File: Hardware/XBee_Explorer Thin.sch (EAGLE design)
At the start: 65 parts, among them J4 QWIIC_RIGHT_ANGLE, Q2 3.1A/30V/105mΩ, U1 FSUSB30MUX_MSOP10, U2 AP63203, U3 ESD Diode, U5 ESD Diode, U6 CP210X

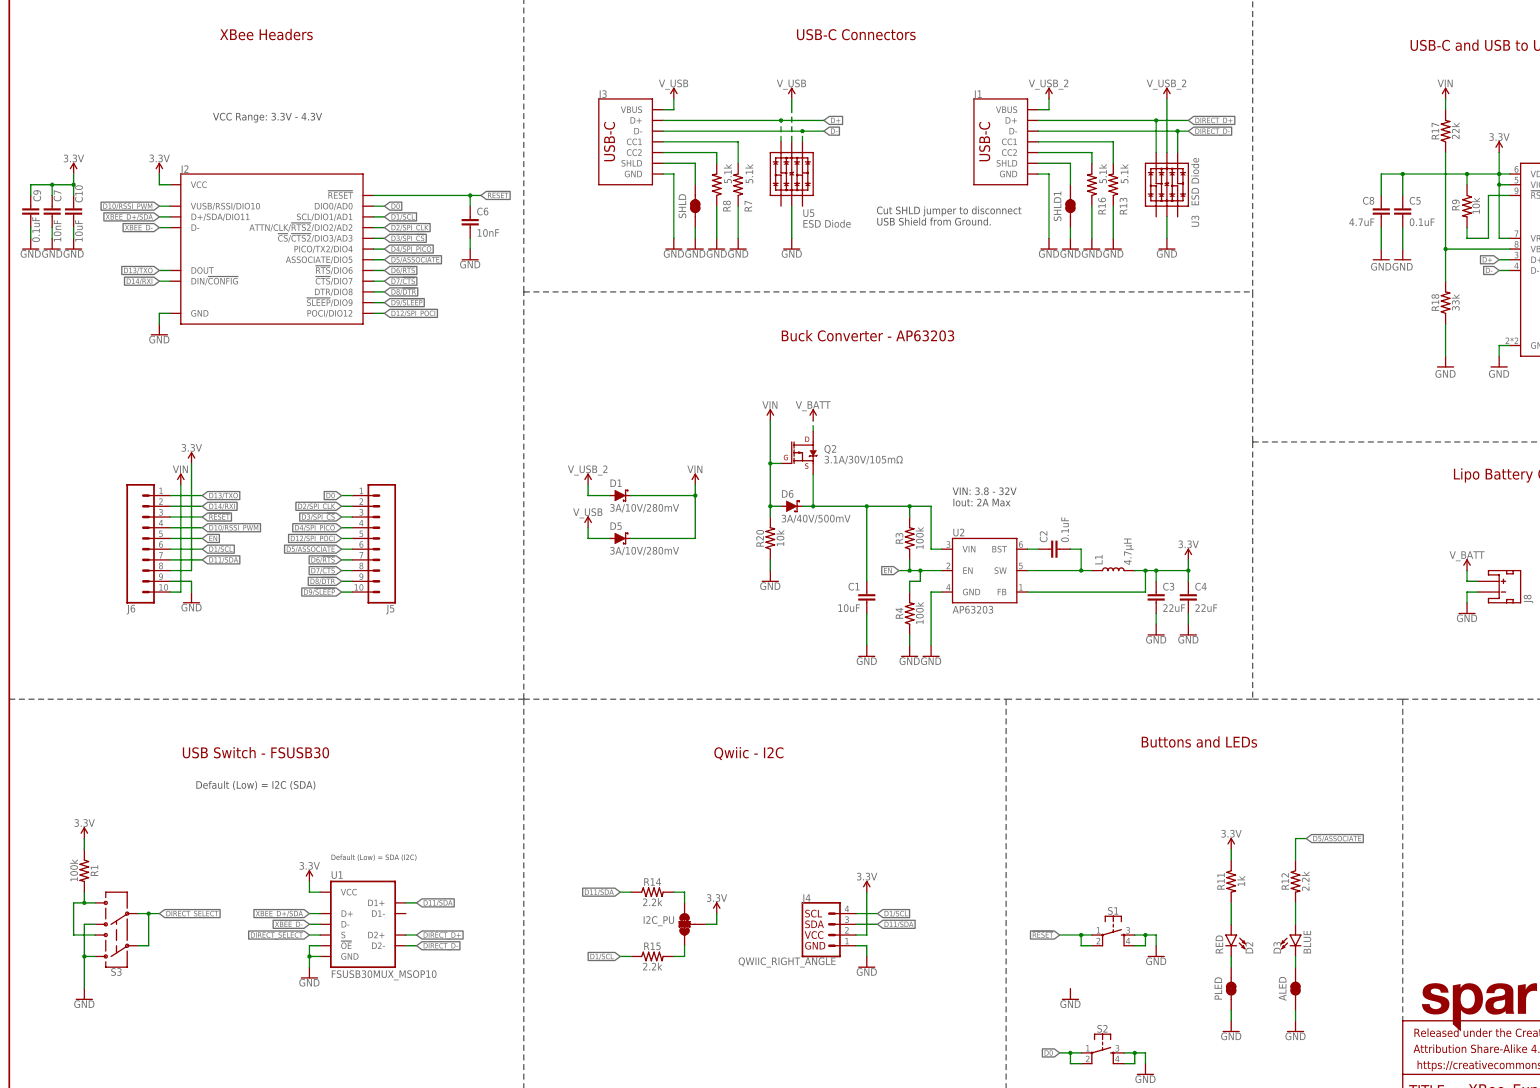
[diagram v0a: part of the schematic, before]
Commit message: Fixes various schematic issues
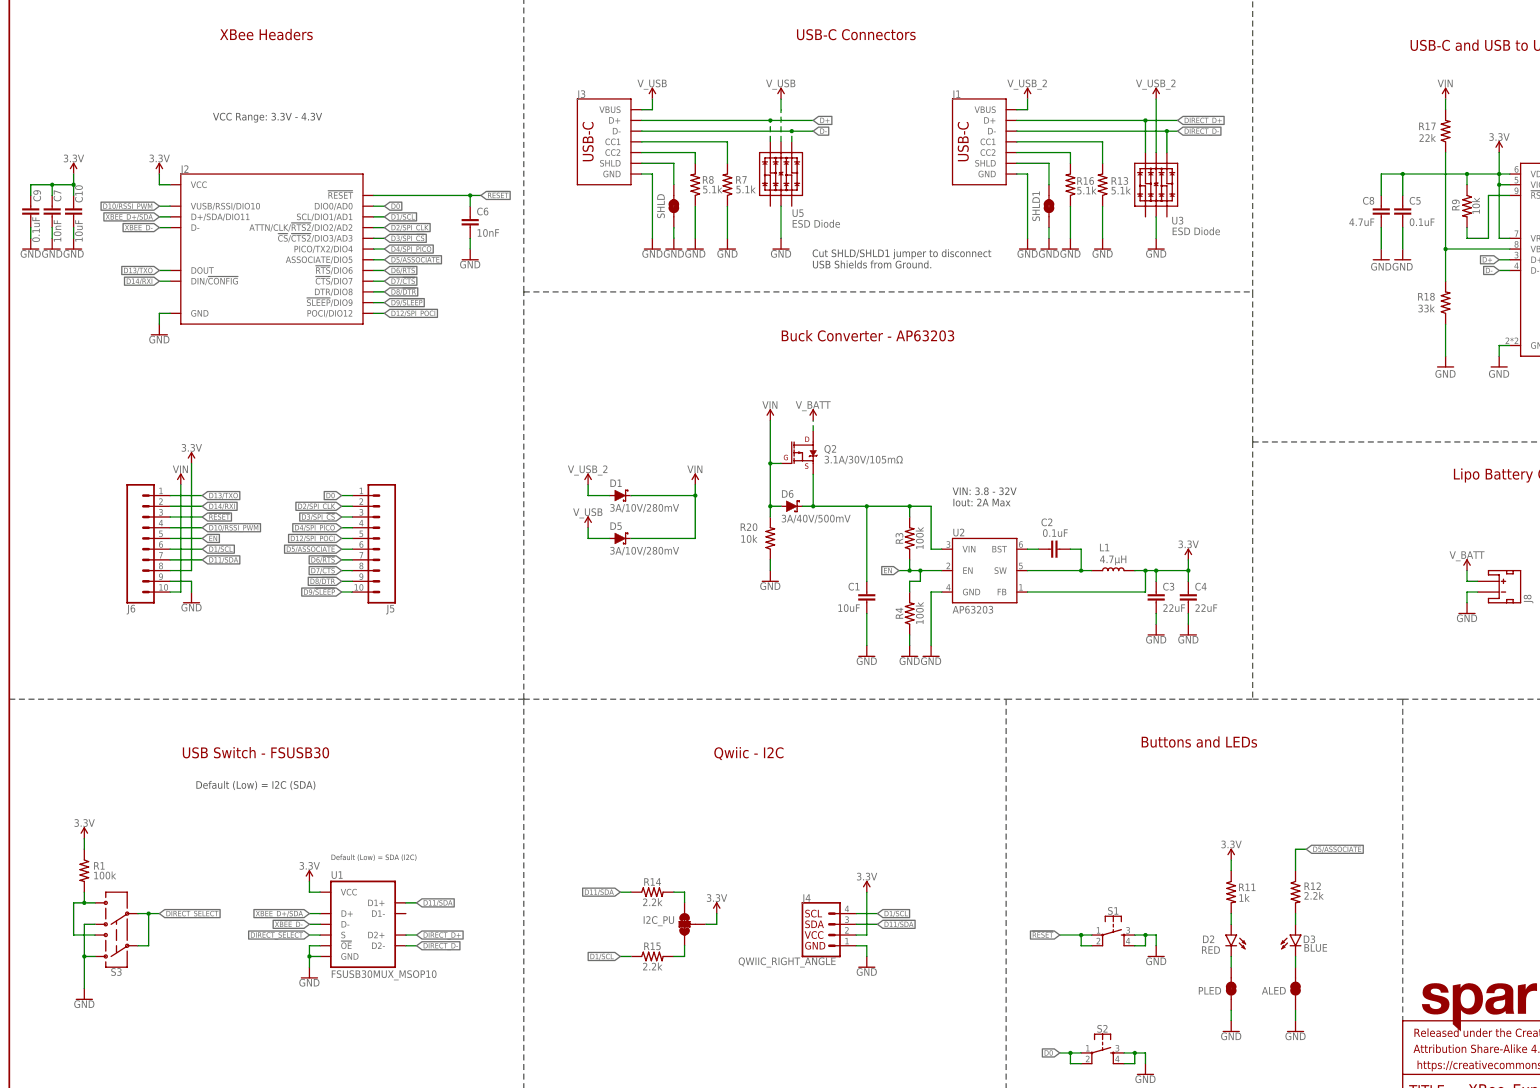
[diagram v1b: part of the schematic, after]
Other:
- note added: "Cut SHLD/SHLD1 jumper to disconnect USB Shields from Ground."
- note removed: "Cut SHLD jumper to disconnect USB Shield from Ground."
- moved on the sheet: J1, J3, R11, R12, R13, R16, R7, R8, SHLD, SHLD1, U3, U5

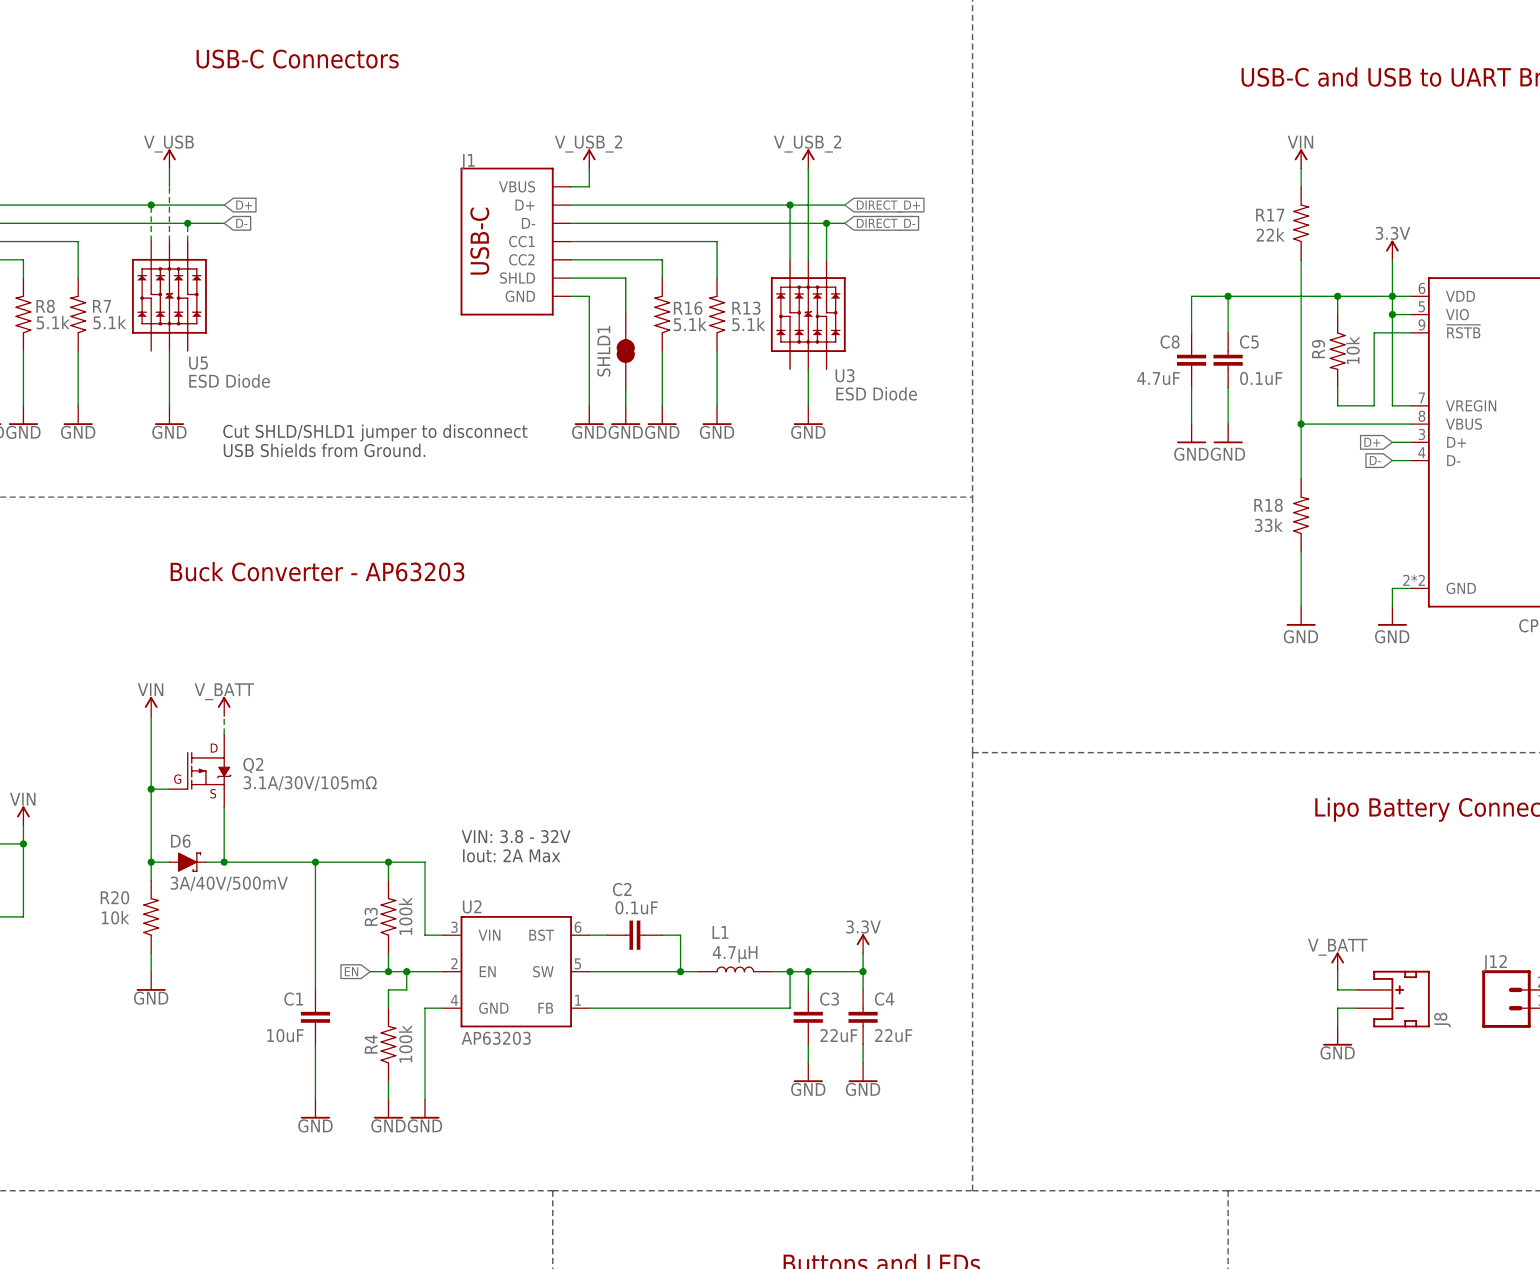
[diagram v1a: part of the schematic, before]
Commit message: Adds more direct feeback trace for feedback pin on regulator
* Restricts ground pour underneath the inductor (which still needs to be changed)
* Updates USB lines to get closer to a 90 ohm impedance (8 mil, 6mil spacing)
* Removes voltage divider on EN pin that was changing the UVLO threshold.
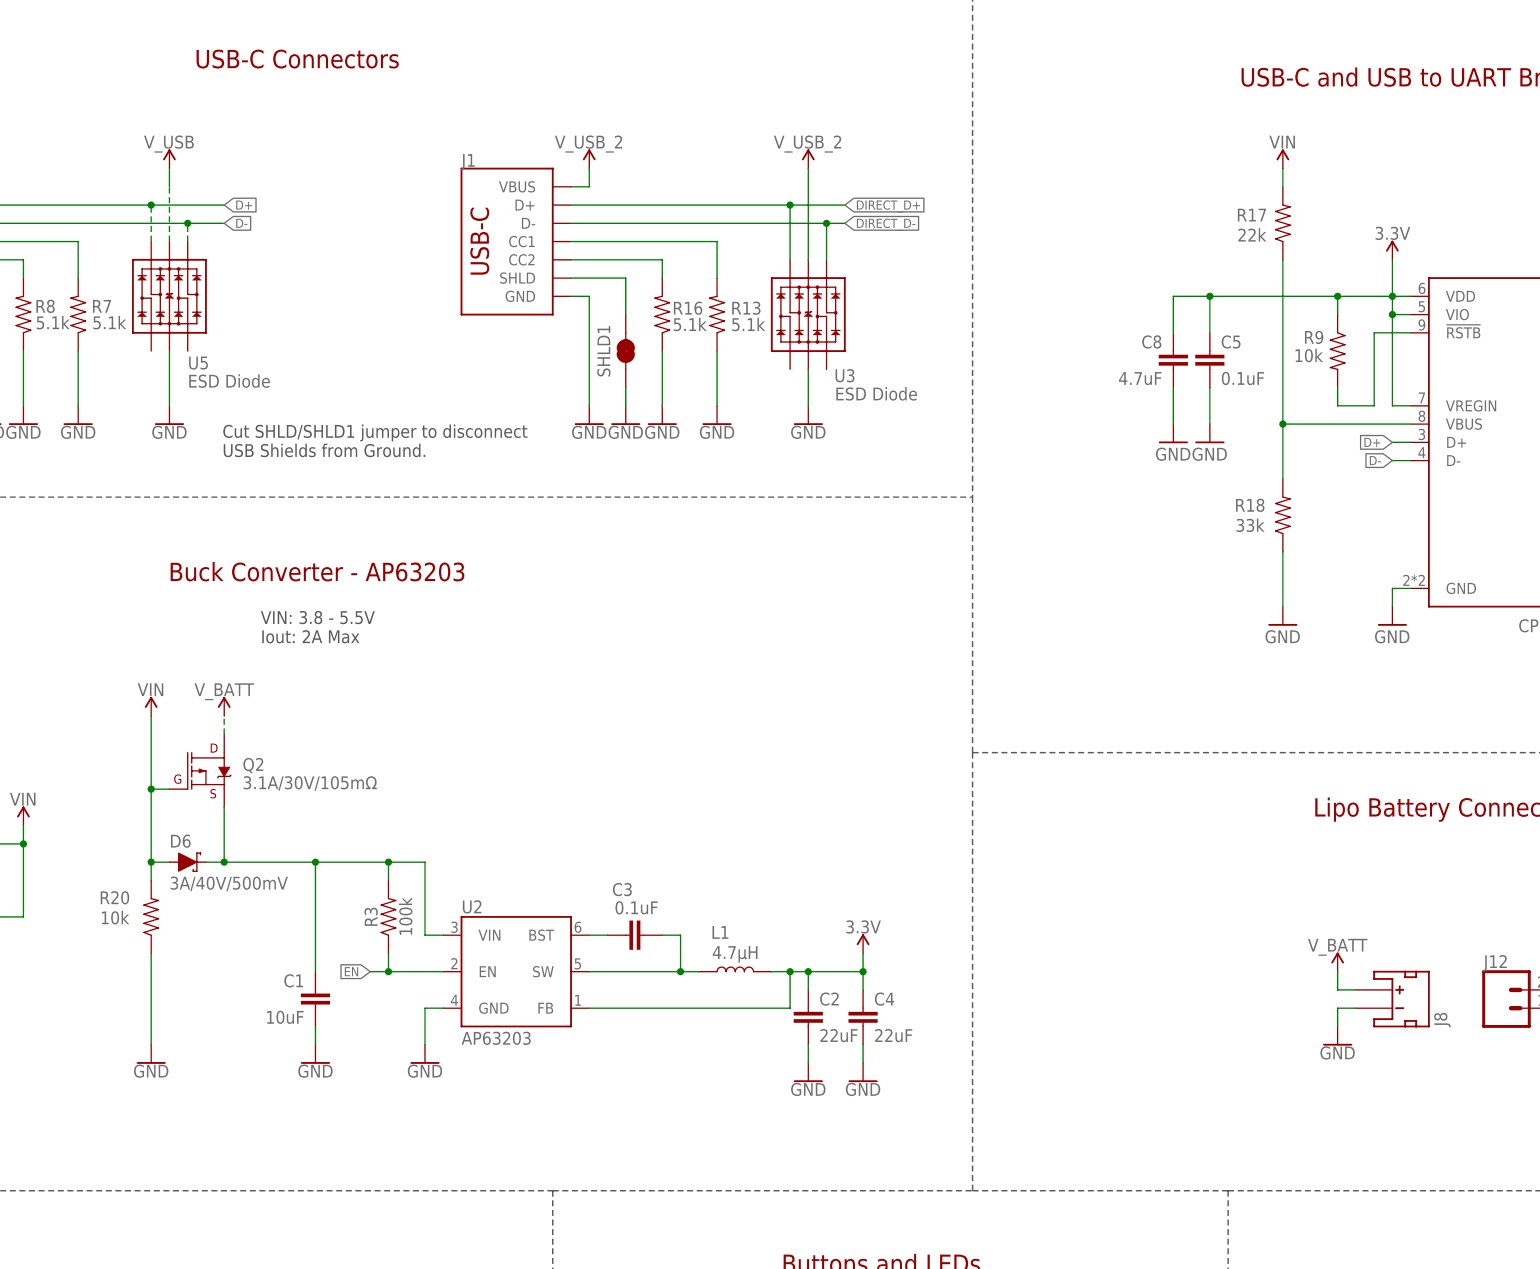
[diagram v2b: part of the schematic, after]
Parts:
- removed R4: 100k, SparkFun-Resistors:100KOHM-0603-1/10W-1%
- C2: value 0.1uF -> 22uF; device SparkFun-Capacitors:0.1UF-0603-25V-5% -> SparkFun-Capacitors:22UF-0603-6.3V-20%
- C3: value 22uF -> 0.1uF; device SparkFun-Capacitors:22UF-0603-6.3V-20% -> SparkFun-Capacitors:0.1UF-0603-25V-5%
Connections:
- net 3.3V: now also C2.1; no longer C3.1
- net EN: no longer R4.2
- net GND: now also C2.2; no longer C3.2, R4.1
- net N$1: now also C3.1; no longer C2.1
- net N$8: now also C3.2; no longer C2.2
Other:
- note added: "VIN: 3.8 - 5.5V Iout: 2A Max"
- note removed: "VIN: 3.8 - 32V Iout: 2A Max"
- moved on the sheet: C1, C2, C3, C5, C8, R17, R18
